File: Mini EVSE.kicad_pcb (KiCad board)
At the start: 2 copper layers, 80 x 60 mm, 34 parts, among them IC1 G3MC-201PL DC5, IC2 IRM-03-5, IC3 ATTINY84-20PU, IC4 RD-0512D, IC5 SI8261BAC-C-IP, J1 RE OUT, J10 M, J2 AC IN, J3 TX, J4 ICP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

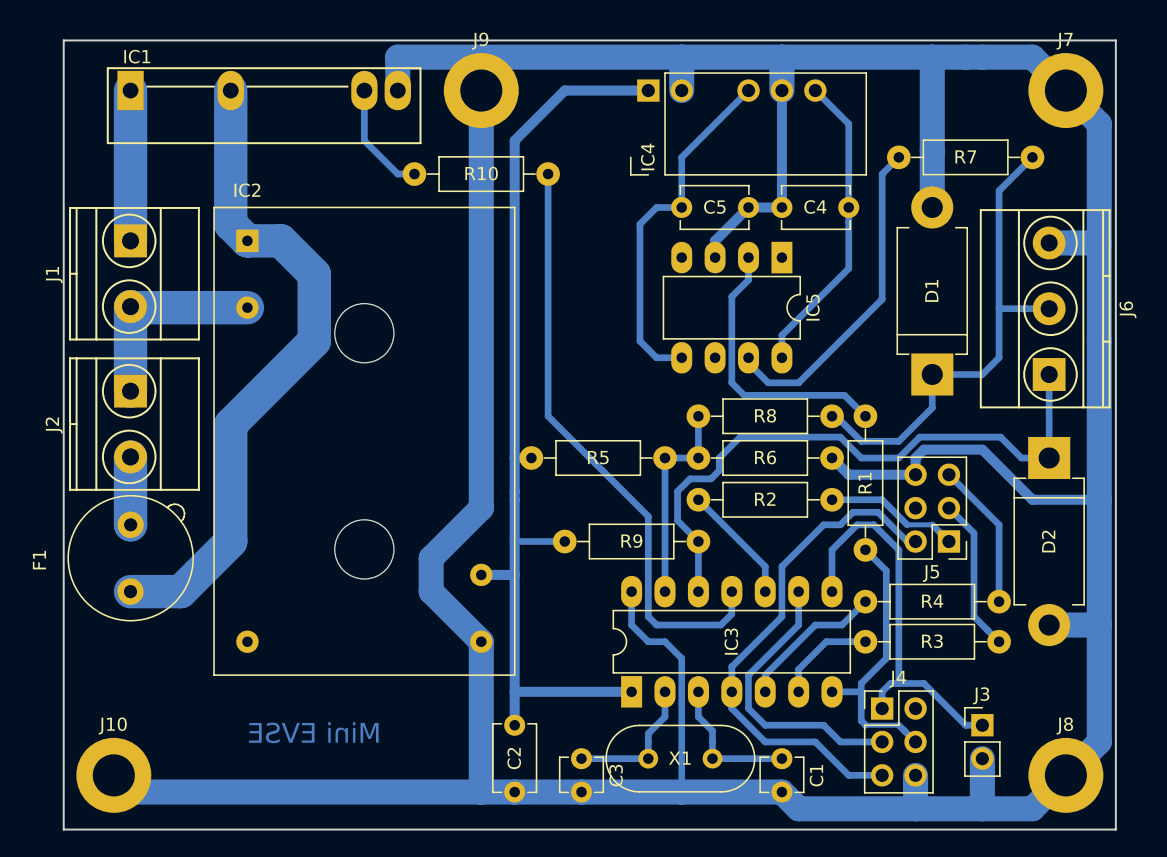
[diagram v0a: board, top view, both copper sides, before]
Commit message: Redone PCB design, now 60x70mm. A few schematics changes to make PCB routing easier.
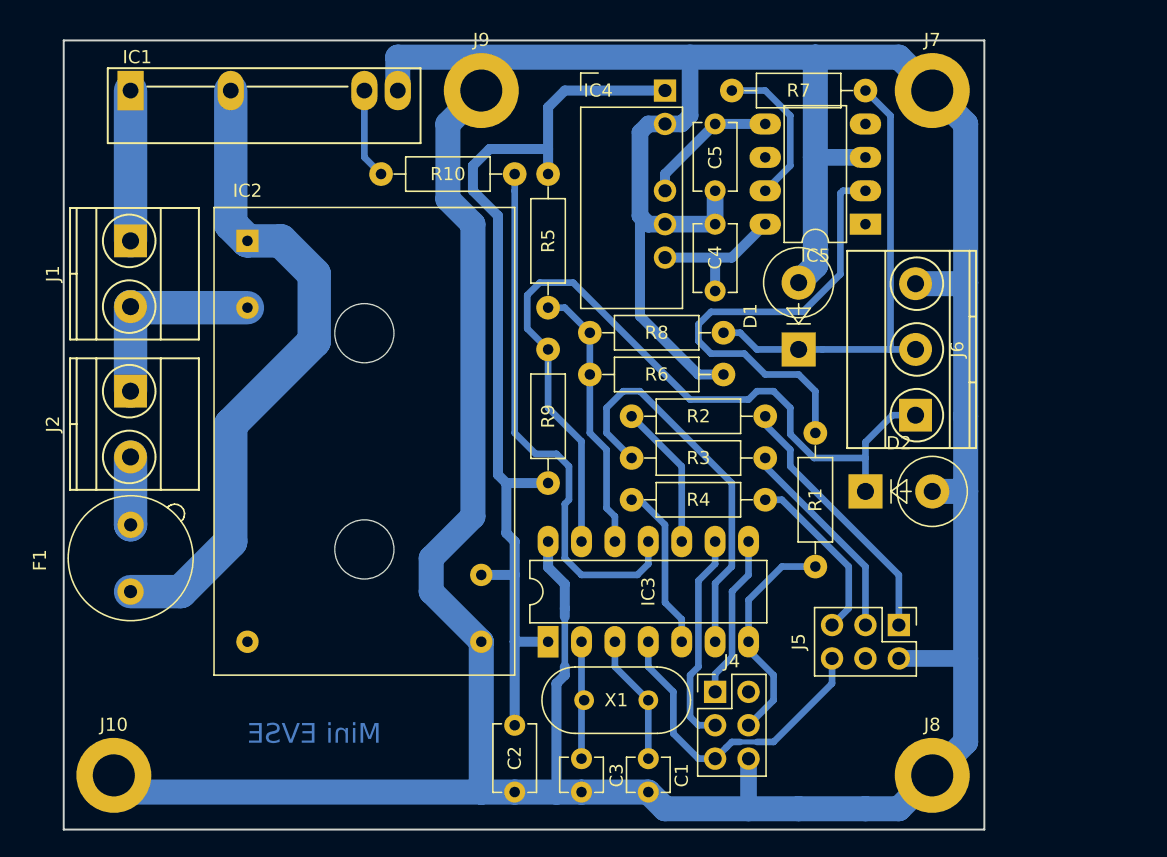
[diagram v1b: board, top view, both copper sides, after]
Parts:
- removed J3: TX, Pin_Headers:Pin_Header_Straight_1x02_Pitch2.54mm
- D1, D2: footprint Diodes_THT:D_DO-201AD_P12.70mm_Horizontal -> Diodes_THT:D_DO-201_P5.08mm_Vertical_KathodeUp
- moved R3 22.6 mm to (116.8, 82.5)
- moved R5 21.6 mm to (100.3, 61.0), turned to 270 degrees
- moved R4 19.4 mm to (116.8, 85.7)
- moved D2 14.2 mm to (124.5, 85.1), turned to 0 degrees
- moved R7 13.7 mm to (124.5, 54.6)
- moved J4 12.8 mm to (113.0, 100.3)
- moved C4 12.0 mm to (113.0, 69.8), turned to 90 degrees
- moved J6 10.6 mm to (128.3, 79.3)
- moved R6 10.4 mm to (103.5, 76.2)
- moved R8 10.4 mm to (113.7, 73.0)
- moved D1 10.3 mm to (119.4, 74.3)
- moved C1 10.2 mm to (108.0, 105.4)
- moved J7 10.2 mm to (129.5, 54.6)
- moved J8 10.2 mm to (129.5, 106.7)
- moved R2 8.13 mm to (116.8, 79.4)
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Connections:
- IC3 pad 12: /PP_MEAS -> /CP_MEAS
- IC3 pad 13: /CP_MEAS -> /PP_MEAS
- J5 pad 2: /SW -> GND
- J5 pad 6: GND -> /SW
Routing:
- net /LED_G: track 7.66 -> 30.1 mm
- net /PA5: track 30.9 -> 12.9 mm
- net -12V: track 27.3 -> 10.5 mm
- net /PP_MEAS: track 47.1 -> 62.2 mm
- net Net-(IC5-Pad2): track 21.3 -> 35.4 mm
- net /SW: track 38.7 -> 24.9 mm
- net Net-(IC5-Pad7): track 25.1 -> 11.7 mm
- net +12V: track 23.5 -> 11.2 mm
- net GND: track 330.4 -> 319.4 mm
- net Net-(J5-Pad1): track 10.2 -> 20.1 mm
- net /SCK: track 21.7 -> 16.3 mm
- net /CP_MEAS: track 15.9 -> 21.0 mm
- net /CH_ON: track 45.5 -> 40.9 mm
- net /CP_OUT: track 21.5 -> 17.2 mm
- net Net-(J5-Pad3): track 11.7 -> 15.9 mm
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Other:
- board size 80 x 60 mm -> 70 x 60 mm

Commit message: Changed DC/DC converter to TMR1-0522
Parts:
- IC4: value RD-0512D -> TMR1-0522
- R5: value 41k3 -> 41k2
- moved IC4 14.3 mm to (109.2, 67.9), turned to 180 degrees
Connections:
- IC4 pad 1: +5V -> GND
- IC4 pad 2: GND -> +5V
- IC4 pad 4: -12V -> +12V
- IC4 pad 6: +12V -> -12V
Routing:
- net +12V: track 11.2 -> 19.2 mm
- net GND: track 319.4 -> 327.2 mm
- net +5V: track 72.9 -> 65.5 mm
- net -12V: track 10.5 -> 13.5 mm

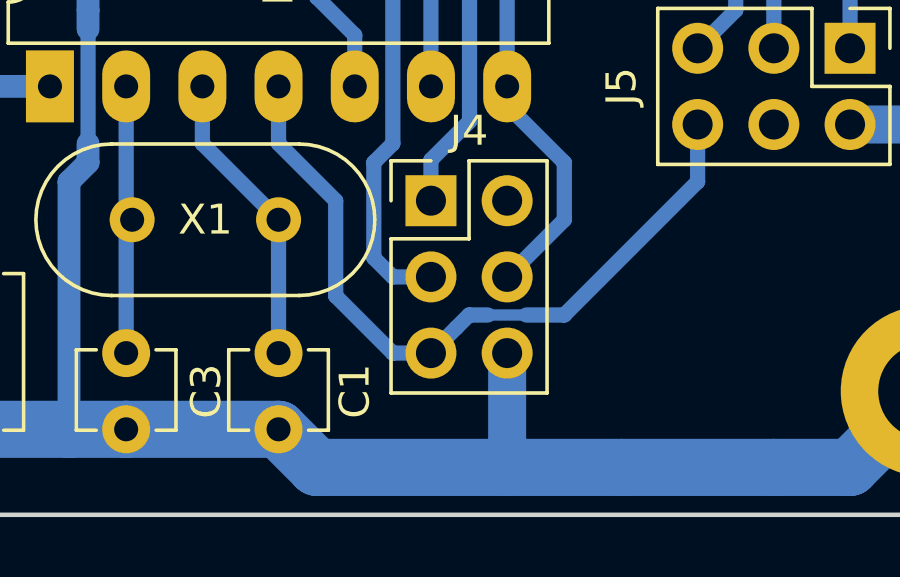
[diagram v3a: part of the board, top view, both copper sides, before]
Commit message: Moved switch from reset pin as we need reset to be active for simple ISP.
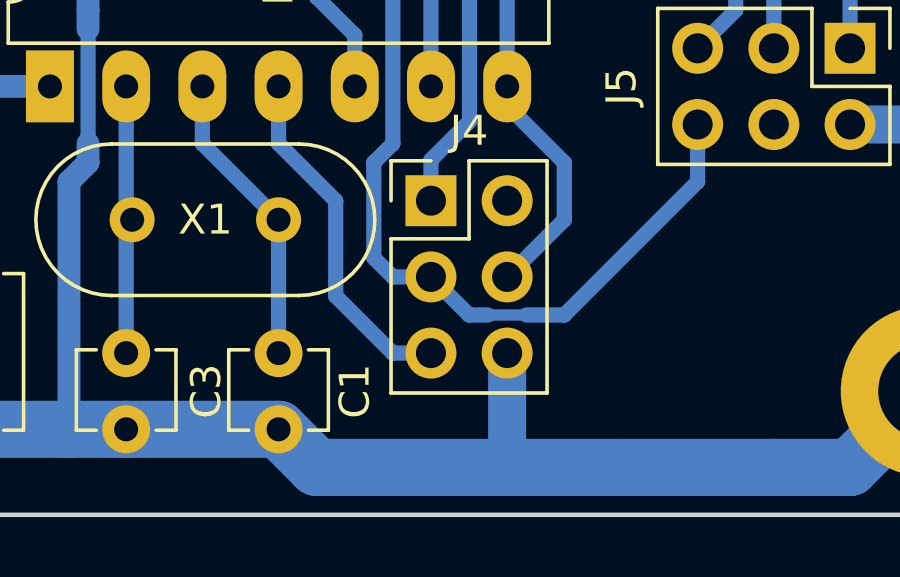
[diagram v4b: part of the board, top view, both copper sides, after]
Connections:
- net /PA5 renamed /MISO
- IC3 pad 4: /SW -> /RESET
- IC3 pad 9: /SCK -> /SW
- J4 pad 3: /SCK -> /SW
- J4 pad 5: /SW -> /RESET
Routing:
- net /SCK: track 16.3 -> 0.00 mm
- net /RESET: track 0.00 -> 11.7 mm
- net /SW: track 24.9 -> 29.5 mm

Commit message: Started working on three-phase setup
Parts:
- moved J4 1.80 mm to (114.3, 101.6)
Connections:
- J5 pad 4: Net-(J5-Pad4) -> +5V
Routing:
- net +5V: track 65.5 -> 95.3 mm
- net /CP_OUT: track 17.2 -> 19.4 mm
- net /RESET: track 11.7 -> 13.5 mm
- net /SW: track 29.5 -> 31.3 mm
- net /MISO: track 12.9 -> 13.6 mm
- net GND: track 327.2 -> 326.7 mm

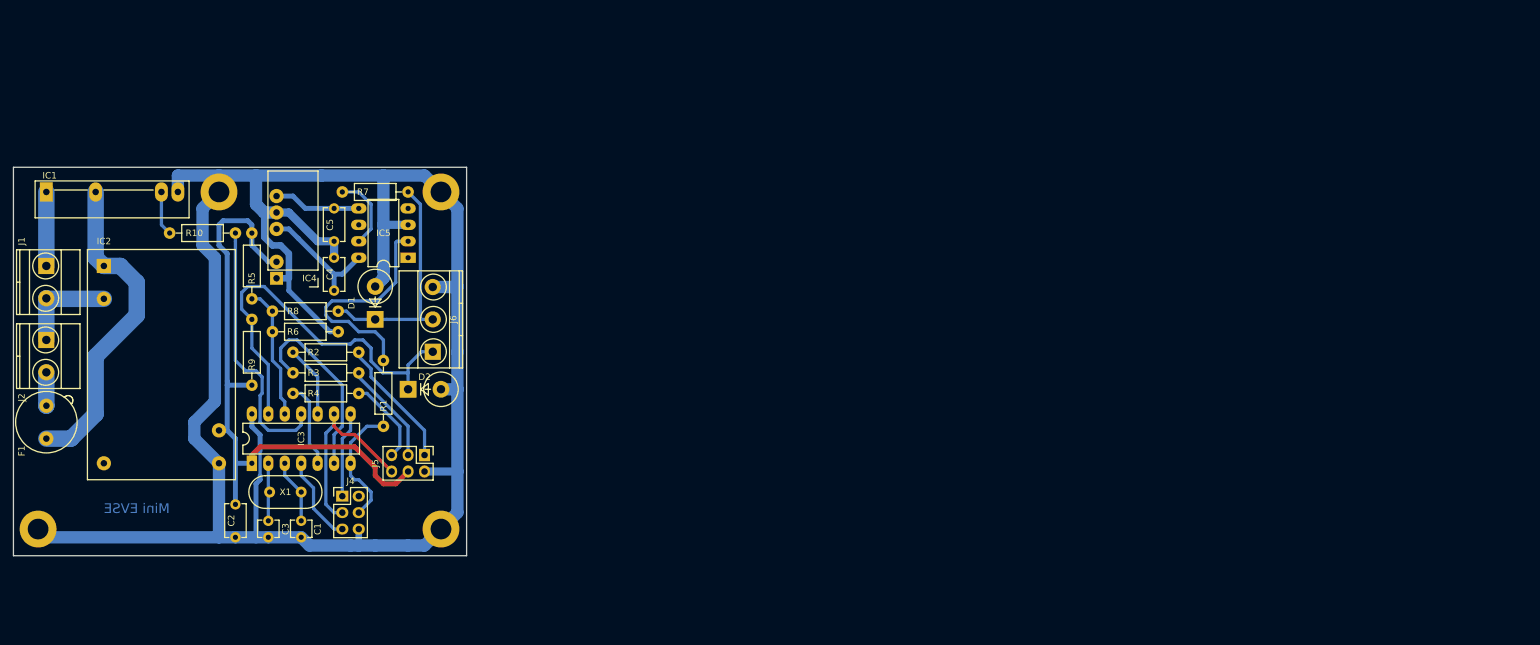
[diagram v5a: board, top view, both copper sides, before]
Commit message: - Switching to SMD - Starting PCB layout
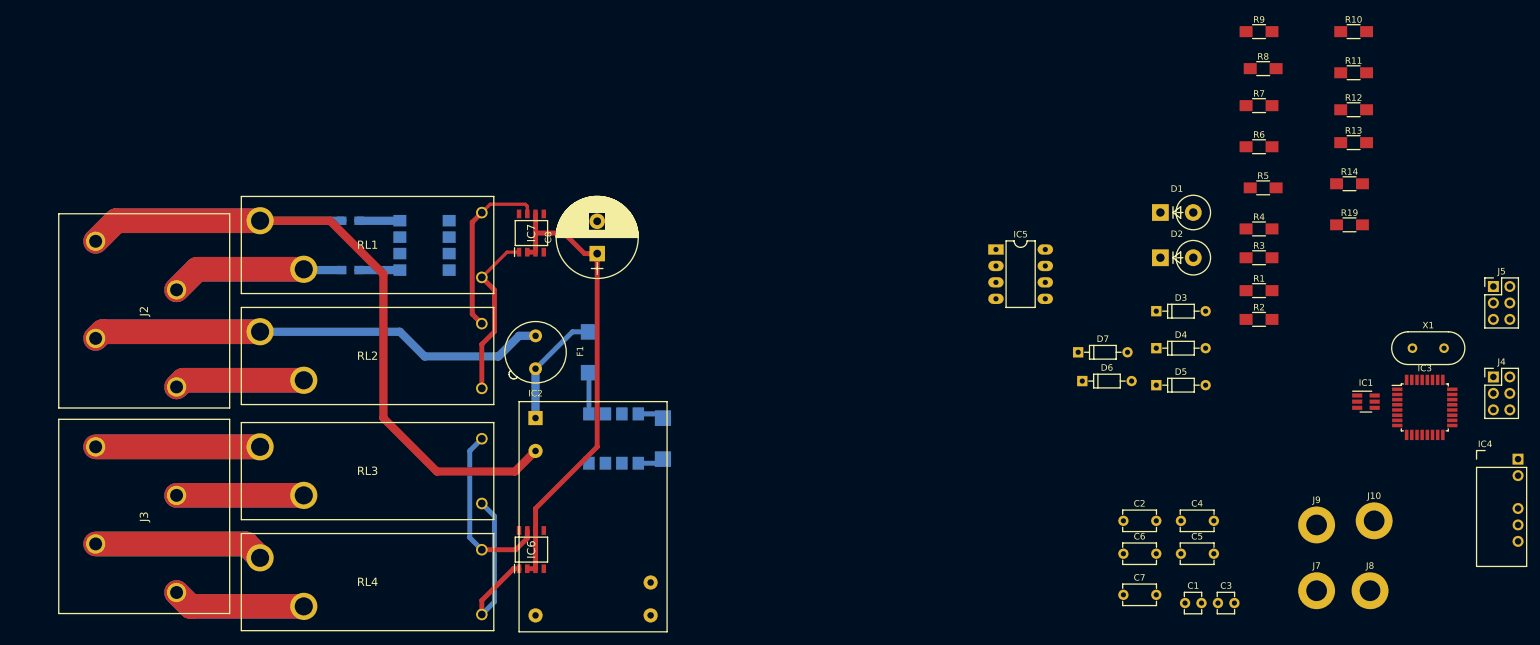
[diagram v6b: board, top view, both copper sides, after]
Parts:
- removed J1: RE OUT, Connectors_Terminal_Blocks:TerminalBlock_Pheonix_MKDS1.5-2pol
- removed J6: PILOTS, Connectors_Terminal_Blocks:TerminalBlock_Pheonix_MKDS1.5-3pol
- added C6: C_Small, Miscellaneous:C_Disc_D5.1mm_W3.2mm_P5.08mm, F.Cu at (234.9, 110.5)
- added C7: C_Small, Miscellaneous:C_Disc_D5.1mm_W3.2mm_P5.08mm, F.Cu at (234.9, 116.8)
- added C8: 0.1F, Capacitors_THT:CP_Radial_D12.5mm_P5.00mm, F.Cu at (153.7, 64.1)
- added D3: D_Schottky, Diodes_THT:D_DO-35_SOD27_P7.62mm_Horizontal, F.Cu at (240.0, 73.0)
- added D4: D_Schottky, Diodes_THT:D_DO-35_SOD27_P7.62mm_Horizontal, F.Cu at (240.0, 78.7)
- added D5: D_Schottky, Diodes_THT:D_DO-35_SOD27_P7.62mm_Horizontal, F.Cu at (240.0, 84.5)
- added D6: D_Schottky, Diodes_THT:D_DO-35_SOD27_P7.62mm_Horizontal, F.Cu at (228.6, 83.8)
- added D7: D, Diodes_THT:D_DO-35_SOD27_P7.62mm_Horizontal, F.Cu at (228.0, 79.4)
- added IC6: BD6211F-E2, SamacSys_Parts:SOIC127P620X160-8N, F.Cu at (143.5, 109.9)
- added IC7: BD6211F-E2, SamacSys_Parts:SOIC127P620X160-8N, F.Cu at (143.5, 61.0)
- added IC8: HCPL3700, Housings_DIP:SMDIP-8_W7.62mm, B.Cu at (127.0, 62.9)
- added IC9: HCPL3700, Housings_DIP:SMDIP-8_W7.62mm, B.Cu at (156.2, 92.7)
- added J3: AC OUT, SamacSys_Parts:1792245, F.Cu at (76.2, 94.0)
- added R11: 10k, Resistors_SMD:R_1206_HandSoldering, F.Cu at (270.5, 36.2)
- added R12: 10k, Resistors_SMD:R_1206_HandSoldering, F.Cu at (270.5, 41.9)
- added R13: 10k, Resistors_SMD:R_1206_HandSoldering, F.Cu at (270.5, 47.0)
- added R14: R, Resistors_SMD:R_1206_HandSoldering, F.Cu at (269.9, 53.3)
- added R15: 82k, Resistors_SMD:R_0805_HandSoldering, B.Cu at (115.5, 66.7)
- added R16: 82k, Resistors_SMD:R_0805_HandSoldering, B.Cu at (115.5, 59.1)
- added R17: 120k, Resistors_SMD:R_2010_HandSoldering, B.Cu at (152.4, 79.4)
- added R18: 120k, Resistors_SMD:R_2010_HandSoldering, B.Cu at (163.8, 92.7)
- added R19: R, Resistors_SMD:R_1206_HandSoldering, F.Cu at (269.9, 59.7)
- added RL1: ADJH21005, SamacSys_Parts:ADJH21005, F.Cu at (135.8, 57.8)
- added RL2: ADJH21005, SamacSys_Parts:ADJH21005, F.Cu at (135.8, 75.0)
- added RL3: ADJH21005, SamacSys_Parts:ADJH21005, F.Cu at (135.8, 92.7)
- added RL4: ADJH21005, SamacSys_Parts:ADJH21005, F.Cu at (135.8, 109.9)
- IC1: value G3MC-201PL DC5 -> 74LVC2G04; footprint Miscellaneous:SIP4_Omron-SSR_Pitch10.16mm_Straight -> TO_SOT_Packages_SMD:SOT-23-6_Handsoldering
- IC3: value ATTINY84-20PU -> ATMEGA328PB-AU; footprint Housings_DIP:DIP-14_W7.62mm_LongPads -> Housings_QFP:TQFP-32_7x7mm_Pitch0.8mm
- J2: footprint Connectors_Terminal_Blocks:TerminalBlock_Pheonix_MKDS1.5-2pol -> SamacSys_Parts:1792245
- R1, R2, R3, R4, R5, R6, R7, R8, R9: footprint Miscellaneous:R_Axial_DIN0207_L6.3mm_D2.5mm_P10.16mm_Horizontal -> Resistors_SMD:R_1206_HandSoldering
- R10: value 301 -> 10k; footprint Miscellaneous:R_Axial_DIN0207_L6.3mm_D2.5mm_P10.16mm_Horizontal -> Resistors_SMD:R_1206_HandSoldering
- moved IC1 206.4 mm to (272.4, 87.0)
- moved J10 206.4 mm to (273.7, 105.4)
- moved IC4 183.7 mm to (290.8, 95.9), turned to 0 degrees
- moved IC3 181.4 mm to (281.5, 87.9), turned to 0 degrees
- moved J4 178.8 mm to (292.1, 83.2)
- moved J9 177.2 mm to (264.8, 106.0)
- moved R10 175.5 mm to (270.5, 29.8), turned to 0 degrees
- moved X1 173.1 mm to (279.6, 78.7), turned to 0 degrees
- moved J5 167.1 mm to (292.1, 69.2), turned to 0 degrees
- moved R9 164.9 mm to (255.9, 29.8), turned to 0 degrees
- moved R5 156.4 mm to (256.5, 54.0), turned to 0 degrees
- moved R6 155.1 mm to (255.9, 47.6)
- moved J7 148.6 mm to (264.8, 116.2)
- moved R8 147.7 mm to (256.5, 35.6), turned to 0 degrees
- moved C3 147.2 mm to (249.6, 118.1), turned to 0 degrees
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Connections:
- net Net-(IC2-Pad3) renamed /N-IN
- F1 pad 1: Net-(F1-Pad1) -> /L1-IN
- IC1 pad 2: Net-(F1-Pad1) -> GND
- IC1 pad 4: GND -> /OFF34
- IC2 pad 1: Net-(F1-Pad1) -> Net-(F1-Pad2)
- IC3 pad 1: +5V -> /LED_R
- IC3 pad 10: /LED_R -> /LED_B
- IC3 pad 11: /CH_ON -> /SW
- IC3 pad 12: /CP_MEAS -> Net-(IC3-Pad12)
- IC3 pad 13: /PP_MEAS -> /CP_OUT
- IC3 pad 14: GND -> Net-(IC3-Pad14)
- IC3 pad 2: /XTAL1 -> Net-(IC3-Pad2)
- IC3 pad 3: /XTAL2 -> /ON12
- IC3 pad 4: /RESET -> +5V
- IC3 pad 5: /LED_B -> GND
- IC3 pad 6: /LED_G -> Net-(IC1-Pad1)
- IC3 pad 7: /CP_OUT -> /XTAL1
- IC3 pad 8: /MISO -> /XTAL2
- IC3 pad 9: /SW -> /LED_G
- J2 pad 2: Net-(F1-Pad2) -> /N-OUT
- J4 pad 3: /SW -> /SCK
- J4 pad 4: /CP_OUT -> /MOSI
- R10 pad 1: /CH_ON -> GND
- R10 pad 2: Net-(IC1-Pad3) -> /ON12
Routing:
- net GND: track 326.7 -> 4.08 mm
- net /N-IN: track 15.4 -> 139.1 mm
- net /L1-IN: track 0.00 -> 97.1 mm
- net +5V: track 95.3 -> 0.00 mm
- net +5C: track 0.00 -> 71.9 mm
- net /PP_MEAS: track 62.2 -> 0.00 mm
- net /L3-IN: track 0.00 -> 52.6 mm
- net /L2-IN: track 0.00 -> 50.8 mm
- net Net-(F1-Pad1): track 50.2 -> 0.00 mm
- net /N-OUT: track 0.00 -> 47.8 mm
- net /L3-OUT: track 0.00 -> 41.1 mm
- net /CH_ON: track 40.9 -> 0.00 mm
- net /L1-OUT: track 0.00 -> 40.2 mm
- net /L2-OUT: track 0.00 -> 39.3 mm
- net Net-(D1-Pad1): track 35.6 -> 0.00 mm
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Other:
- board outline removed
- board text removed: "Mini EVSE"

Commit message: Working on upgrading to KiCAD 6
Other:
- net class Default removed
